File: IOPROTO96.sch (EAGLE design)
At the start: 4 parts

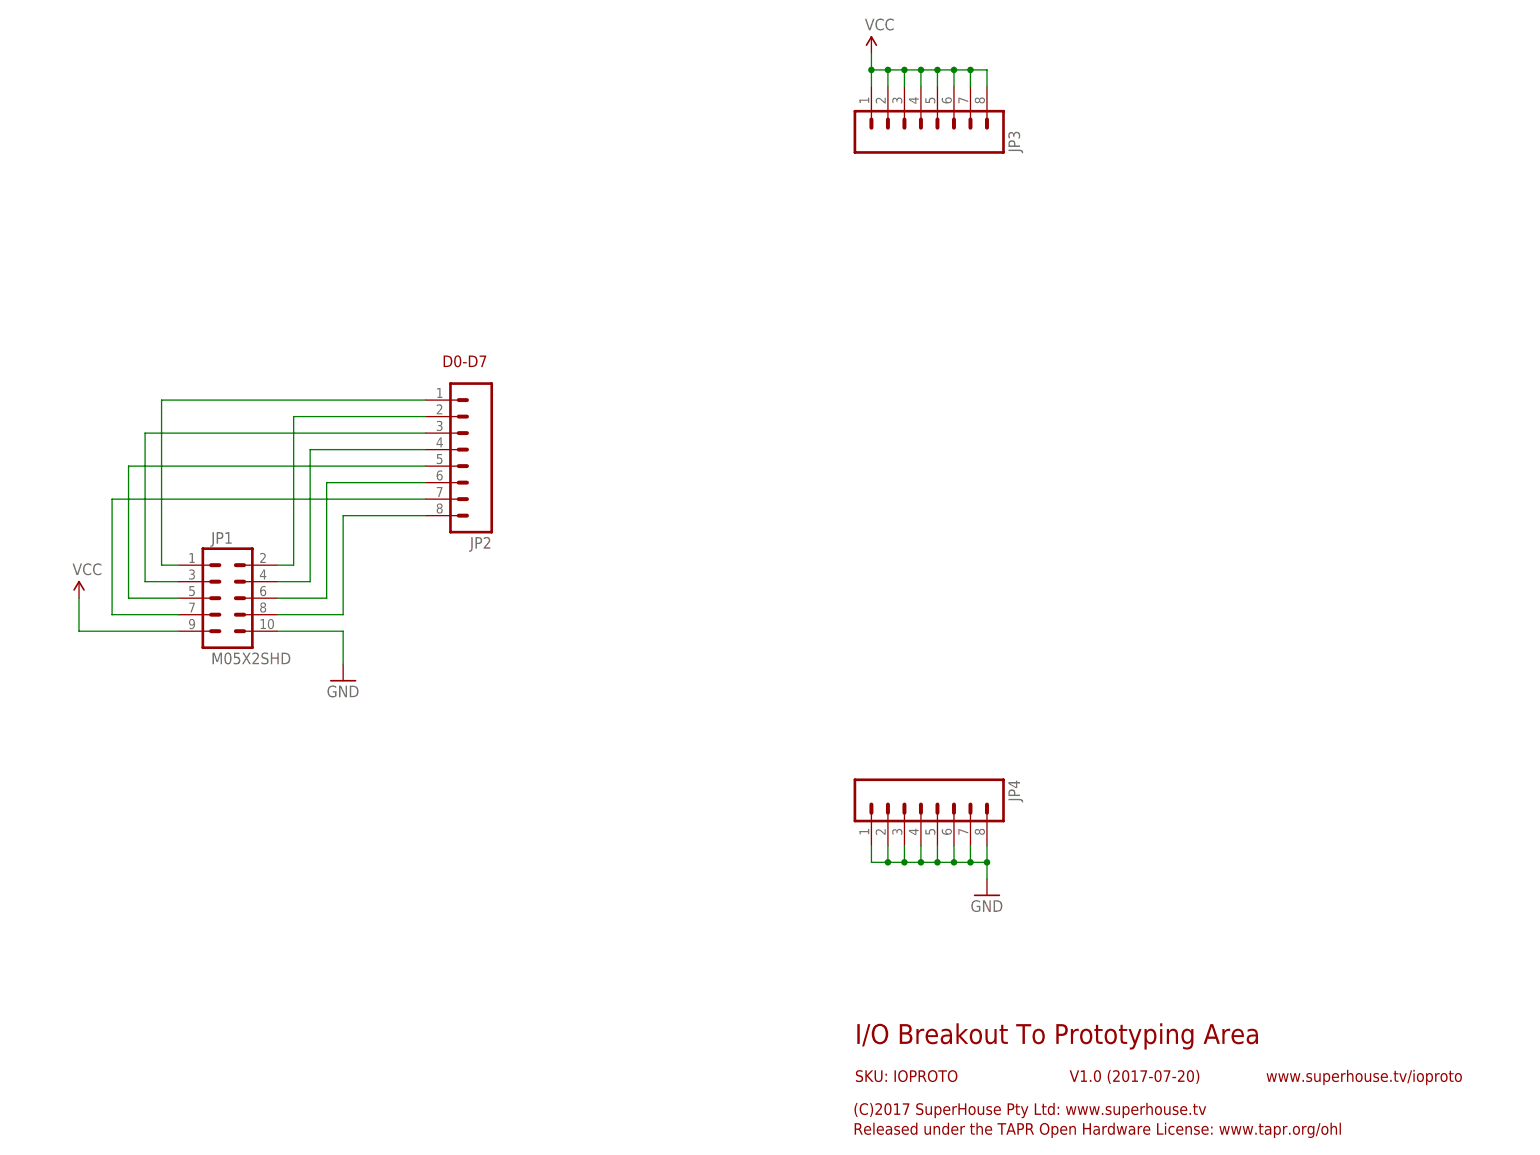
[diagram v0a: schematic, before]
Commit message: Updated silkscreen for v2.0 release
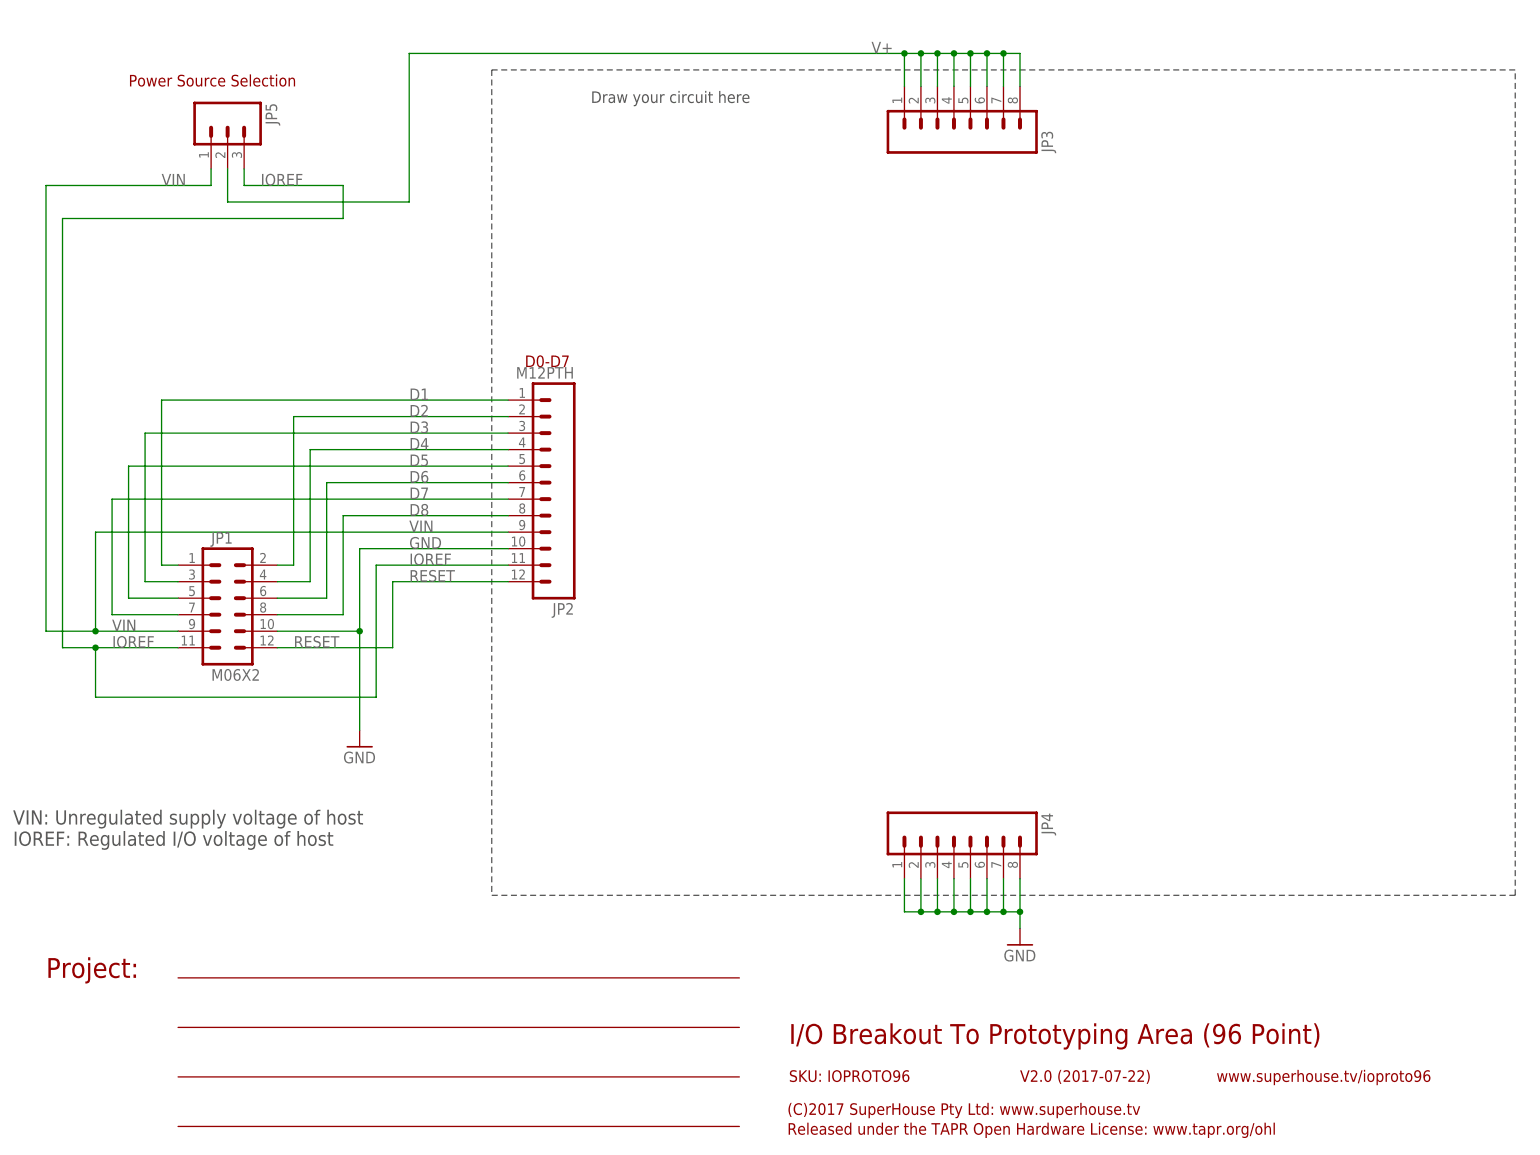
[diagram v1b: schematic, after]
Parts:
- added JP5: (no value), freetronics-jon:M03PTH
- JP1: value M05X2SHD -> M06X2; device freetronics-original:M05X2SHD -> freetronics-jon:M06X2
- JP2: value (none) -> M12PTH; device freetronics-master-v1:M08 -> freetronics-original:M12PTH
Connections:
- net N$11 renamed D5
- net N$12 renamed D3
- net N$13 renamed D1
- net N$14 renamed D7
- net N$27 renamed D8
- net N$28 renamed D6
- net N$29 renamed D4
- net N$30 renamed D2
- removed net VCC: JP1.9, JP3.1, JP3.2, JP3.3, JP3.4, JP3.5, JP3.6, JP3.7, JP3.8
- new net IOREF: JP1.11, JP2.11, JP5.3
- new net RESET: JP1.12, JP2.12
- new net V+: JP3.1, JP3.2, JP3.3, JP3.4, JP3.5, JP3.6, JP3.7, JP3.8, JP5.2
- new net VIN: JP1.9, JP2.9, JP5.1
- net GND: now also JP2.10
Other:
- note added: "Draw your circuit here"
- note added: "I/O Breakout To Prototyping Area (96 Point)"
- note added: "Power Source Selection"
- note added: "Project:"
- note added: "SKU: IOPROTO96"
- note added: "V2.0 (2017-07-22)"
- note added: "VIN: Unregulated supply voltage of host IOREF: Regulated I/O voltage of host"
- note added: "www.superhouse.tv/ioproto96"
- note removed: "I/O Breakout To Prototyping Area"
- note removed: "SKU: IOPROTO"
- note removed: "V1.0 (2017-07-20)"
- note removed: "www.superhouse.tv/ioproto"
- moved on the sheet: JP3, JP4

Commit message: Final routing and DRC for release v2.0
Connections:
- net D1 renamed IO1
- net D2 renamed IO2
- net D3 renamed IO3
- net D4 renamed IO4
- net D5 renamed IO5
- net D6 renamed IO6
- net D7 renamed IO7
- net D8 renamed IO8
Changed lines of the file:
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@@
 </segment>
 </net>
-<net name="D5" class="0">
+<net name="IO5" class="0">
 <segment>
 <pinref part="JP1" gate="G$1" pin="5"/>
@@
 </segment>
 </net>
-<net name="D3" class="0">
+<net name="IO3" class="0">
 <segment>
 <pinref part="JP1" gate="G$1" pin="3"/>
@@
 </segment>
 </net>
-<net name="D1" class="0">
+<net name="IO1" class="0">
 <segment>
 <pinref part="JP1" gate="G$1" pin="1"/>
@@
 </segment>
 </net>
-<net name="D7" class="0">
+<net name="IO7" class="0">
 <segment>
 <pinref part="JP1" gate="G$1" pin="7"/>
@@
 </segment>
 </net>
-<net name="D8" class="0">
+<net name="IO8" class="0">
 <segment>
 <pinref part="JP1" gate="G$1" pin="8"/>
@@
 </segment>
 </net>
-<net name="D6" class="0">
+<net name="IO6" class="0">
 <segment>
 <pinref part="JP1" gate="G$1" pin="6"/>
@@
 </segment>
 </net>
-<net name="D4" class="0">
+<net name="IO4" class="0">
 <segment>
 <pinref part="JP1" gate="G$1" pin="4"/>
@@
 </segment>
 </net>
-<net name="D2" class="0">
+<net name="IO2" class="0">
 <segment>
 <pinref part="JP1" gate="G$1" pin="2"/>
